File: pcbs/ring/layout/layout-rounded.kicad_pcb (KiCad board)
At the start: 2 copper layers, 56 x 6.2 mm, 60 parts, among them J1 ?, Q1 CSD13380F3T, Q2 CSD13380F3T, U1 BQ27427YZFR, U2 BQ29700, U3 nRF52833-QDAA, U4 MAX30102EFD+T, U5 LSM6DSOX, U6 ?, U7 TMP117AIDRVR, U8 TPS7A2018PDQN, Y1 8J32076001, Y2 3110M4-32.768DTTLLLL

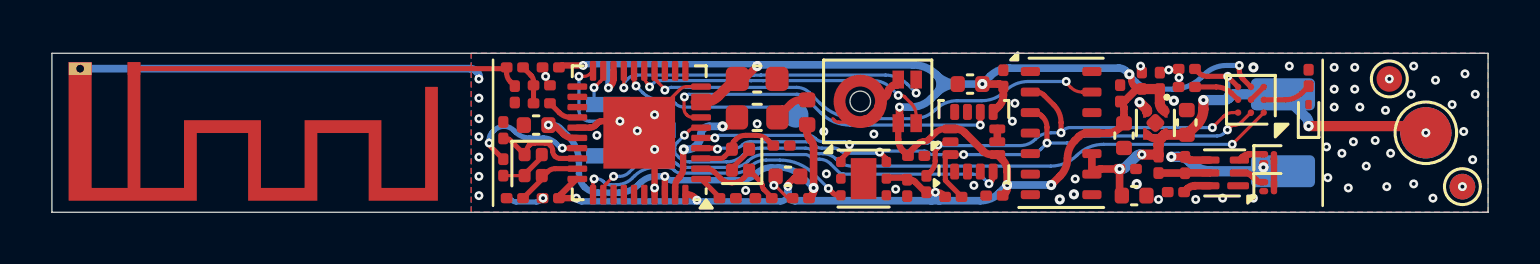
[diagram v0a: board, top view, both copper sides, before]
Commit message: stricter DRC
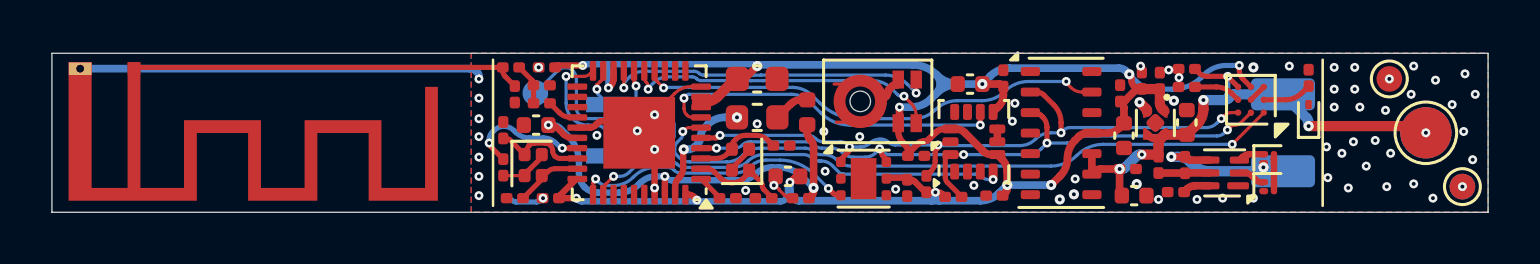
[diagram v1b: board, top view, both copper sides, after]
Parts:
- moved TP1 10.2 mm to (137.1, 81.5)
- moved L4 0.15 mm to (136.2, 80.5)
- moved C8 0.15 mm to (137.6, 80.5)
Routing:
- net GND: track 35.5 -> 36.7 mm, vias 68 -> 67
- net swdclk: track 4.55 -> 5.29 mm
- net rst: track 7.18 -> 7.71 mm

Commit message: stricterer DRC
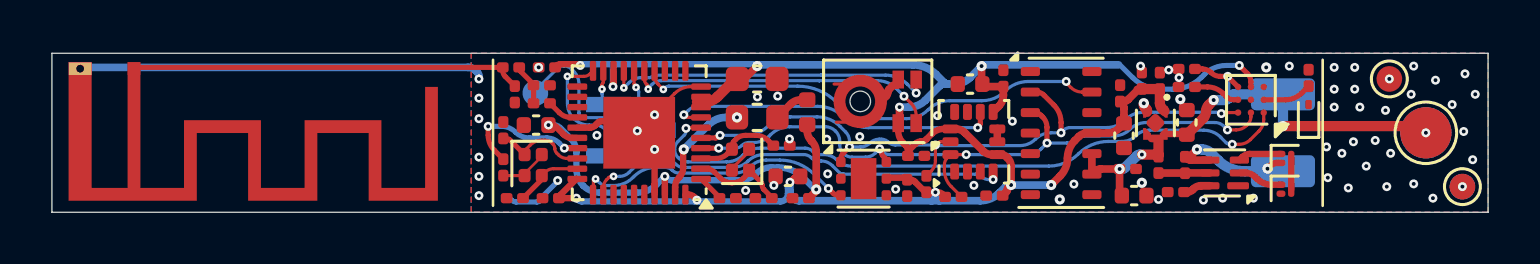
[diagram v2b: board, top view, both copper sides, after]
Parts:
- moved Q2 0.68 mm to (166.3, 85.3)
- moved Q1 0.68 mm to (166.3, 84.1)
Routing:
- net sda: track 27.0 -> 28.3 mm
- net VDD: track 82.0 -> 81.1 mm, vias 13 -> 12
- net imu_int2: track 13.8 -> 13.1 mm
- net battery.bat_cout: track 1.06 -> 1.75 mm
- net battery.bat_dout: track 1.02 -> 1.70 mm
- net VBATT: track 21.1 -> 20.5 mm
- net scl: track 26.5 -> 27.1 mm
- net bat_low: track 25.8 -> 26.4 mm
- net battery.bat_vss: track 6.21 -> 5.70 mm
- net GND: track 36.7 -> 36.3 mm, vias 67 -> 66
